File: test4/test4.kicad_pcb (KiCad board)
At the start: 4 copper layers, 26.7 x 16.3 mm, 2 parts, among them U1 74LS245, U2 74LS245

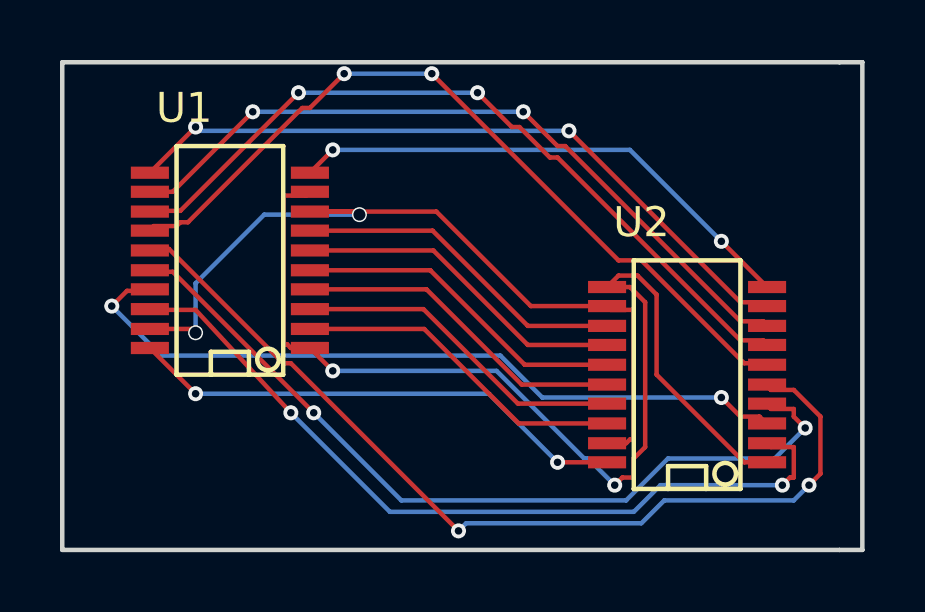
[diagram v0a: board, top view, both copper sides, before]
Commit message: test4 is routed with planes
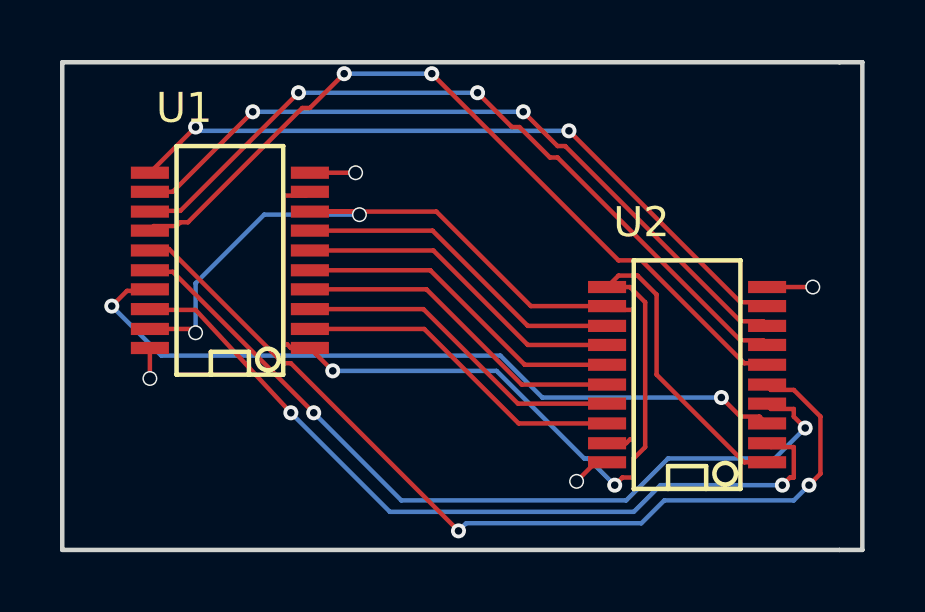
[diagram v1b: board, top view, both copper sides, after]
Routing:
- net GND: track 17.4 -> 3.05 mm
- net +3V3: track 16.8 -> 2.42 mm
- added copper zone on In2.Cu, net +3V3
- added copper zone on In1.Cu, net GND
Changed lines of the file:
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@@
     (links 22)
     (no_connects 0)
-    (area 128.905 90.551 155.829 107.188)
+    (area 128.956999 90.662999 155.777001 107.263001)
     (thickness 1.6)
     (drawings 6)
-    (tracks 183)
+    (tracks 181)
     (zones 0)
     (modules 2)
@@
     (0 F.Cu signal)
     (1 In1.Cu power)
-    (2 In2.Cu power)
+    (2 In2.Cu power hide)
     (31 B.Cu signal)
     (32 B.Adhes user)
@@
     (trace_clearance 0.15)
     (zone_clearance 0.508)
-    (zone_45_only no)
+    (zone_45_only yes)
     (trace_min 0.15)
     (segment_width 0.2)
@@
   (segment (start 141.3764 96.5454) (end 137.287 96.5454) (width 0.15) (layer F.Cu) (net 7) (status 20))
   (segment (start 144.5514 99.7204) (end 141.3764 96.5454) (width 0.15) (layer F.Cu) (net 7))
-  (segment (start 137.287 95.9104) (end 138.8364 95.9104) (width 0.15) (layer F.Cu) (net 8) (status 400000))
-  (segment (start 133.35 99.822) (end 131.953 99.822) (width 0.15) (layer F.Cu) (net 8) (status 800000))
+  (segment (start 137.287 95.9104) (end 138.8364 95.9104) (width 0.15) (layer F.Cu) (net 8) (status 10))
+  (segment (start 133.35 99.822) (end 131.953 99.822) (width 0.15) (layer F.Cu) (net 8) (status 20))
   (segment (start 133.477 99.949) (end 133.35 99.822) (width 0.15) (layer F.Cu) (net 8))
   (via (at 133.477 99.949) (size 0.5) (drill 0.4) (layers F.Cu B.Cu) (net 8))
@@
   (segment (start 141.5034 95.9104) (end 137.287 95.9104) (width 0.15) (layer F.Cu) (net 8) (status 20))
   (segment (start 144.653 99.06) (end 141.5034 95.9104) (width 0.15) (layer F.Cu) (net 8))
-  (segment (start 152.527 98.425) (end 151.003 96.901) (width 0.15) (layer F.Cu) (net 9) (status 80010))
-  (via (at 151.003 96.901) (size 0.5) (layers F.Cu B.Cu) (net 9) (status 80000))
-  (segment (start 151.003 96.901) (end 147.955 93.853) (width 0.15) (layer B.Cu) (net 9) (status 80000))
-  (segment (start 147.955 93.853) (end 138.049 93.853) (width 0.15) (layer B.Cu) (net 9) (status 80000))
-  (via (at 138.049 93.853) (size 0.5) (layers F.Cu B.Cu) (net 9) (status 80000))
-  (segment (start 138.049 93.853) (end 137.287 94.615) (width 0.15) (layer F.Cu) (net 9) (status 80020))
+  (segment (start 152.527 98.425) (end 154.051 98.425) (width 0.15) (layer F.Cu) (net 9))
+  (via (at 154.051 98.425) (size 0.5) (drill 0.4) (layers F.Cu B.Cu) (net 9))
+  (segment (start 137.287 94.615) (end 138.811 94.615) (width 0.15) (layer F.Cu) (net 9))
+  (via (at 138.811 94.615) (size 0.5) (drill 0.4) (layers F.Cu B.Cu) (net 9))
   (segment (start 131.953 94.615) (end 133.477 93.091) (width 0.15) (layer F.Cu) (net 10) (status 80010))
   (via (at 133.477 93.091) (size 0.5) (layers F.Cu B.Cu) (net 10) (status 80000))
@@
   (segment (start 153.416 103.759) (end 152.654 103.759) (width 0.15) (layer F.Cu) (net 17) (status 80020))
   (segment (start 152.654 103.759) (end 152.527 103.632) (width 0.15) (layer F.Cu) (net 17) (status 80030))
-  (segment (start 147.193 104.267) (end 145.542 104.267) (width 0.15) (layer F.Cu) (net 18) (status 80010))
-  (via (at 145.542 104.267) (size 0.5) (layers F.Cu B.Cu) (net 18) (status 80000))
-  (segment (start 145.542 104.267) (end 143.256 101.981) (width 0.15) (layer B.Cu) (net 18) (status 80000))
-  (segment (start 143.256 101.981) (end 133.477 101.981) (width 0.15) (layer B.Cu) (net 18) (status 80000))
-  (via (at 133.477 101.981) (size 0.5) (layers F.Cu B.Cu) (net 18) (status 80000))
-  (segment (start 133.477 101.981) (end 131.953 100.457) (width 0.15) (layer F.Cu) (net 18) (status 80020))
+  (segment (start 147.193 104.267) (end 146.812 104.267) (width 0.15) (layer F.Cu) (net 18))
+  (segment (start 146.812 104.267) (end 146.177 104.902) (width 0.15) (layer F.Cu) (net 18))
+  (via (at 146.177 104.902) (size 0.5) (drill 0.4) (layers F.Cu B.Cu) (net 18))
+  (segment (start 131.953 100.457) (end 131.953 101.473) (width 0.15) (layer F.Cu) (net 18))
+  (segment (start 131.953 101.473) (end 131.953 101.6) (width 0.15) (layer B.Cu) (net 18))
+  (via (at 131.953 101.473) (size 0.5) (drill 0.4) (layers F.Cu B.Cu) (net 18))
+  (zone (net 9) (net_name GND) (layer In1.Cu) (hatch edge 0.508)
+    (connect_pads (clearance 0.508))
+    (min_thickness 0.254)
+    (fill yes (arc_segments 16) (thermal_gap 0.508) (thermal_bridge_width 0.508))
+    (polygon
+      (pts
+        (xy 129.032 91.059) (xy 129.032 107.188) (xy 155.702 107.188) (xy 155.702 90.932) (xy 129.032 90.932)
+        (xy 129.032 91.059)
+      )
+    )
+  )
+  (zone (net 18) (net_name +3V3) (layer In2.Cu) (hatch edge 0.508)
+    (connect_pads (clearance 0.508))
+    (min_thickness 0.254)
+    (fill yes (arc_segments 16) (thermal_gap 0.508) (thermal_bridge_width 0.508))
+    (polygon
+      (pts
+        (xy 155.702 107.188) (xy 129.032 107.188) (xy 129.032 90.932) (xy 155.702 90.932) (xy 155.702 107.188)
+      )
+    )
+  )
 )
